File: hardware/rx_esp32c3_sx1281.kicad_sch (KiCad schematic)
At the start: 42 parts, among them U1 ESP32-C3, U3 SX1281IMLTRT, X1 CJ17-400001010B20

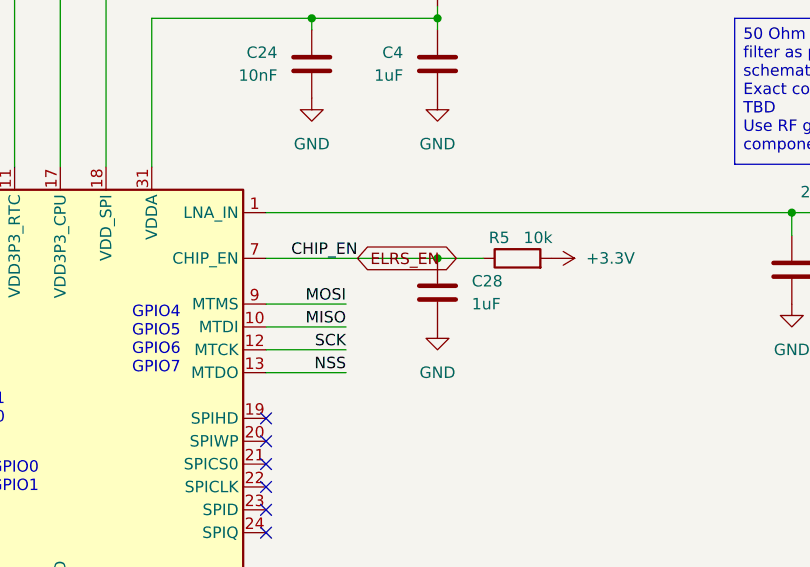
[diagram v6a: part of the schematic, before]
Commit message: ELRS OFF solder jumper JP2 and 1k R115 on CHIP_EN
- JP2 (CHIP_EN to GND, new 1.10 x 0.55 mm footprint
  lib:SolderJumper-2_P0.65mm_Tiny_Open, open mask, no paste): bridging it
  holds the ESP32-C3 in reset with any firmware, so an external receiver on
  J54/J55 or the DJI SBUS on SH-6 pin 6 owns UART1.
- R115 1k between GPIO27 (ELRS_EN) and CHIP_EN: GPIO27 cannot short into a
  bridged jumper (3.3 mA).
- tools/elrs_jumper.py (pcbnew footprint, sexpdata schematic); netlist diff:
  only CHIP_EN/ELRS_EN/GND gain the new pins. ERC 520 -> 519.
- Board synced; JP2, R115, TP42, TP43 parked right of the outline for
  placement (they overlap there: 4 shorting errors until placed).
- R115 has no LCSC number yet.

Co-Authored-By: Claude Opus 5.5 <noreply@anthropic.com>
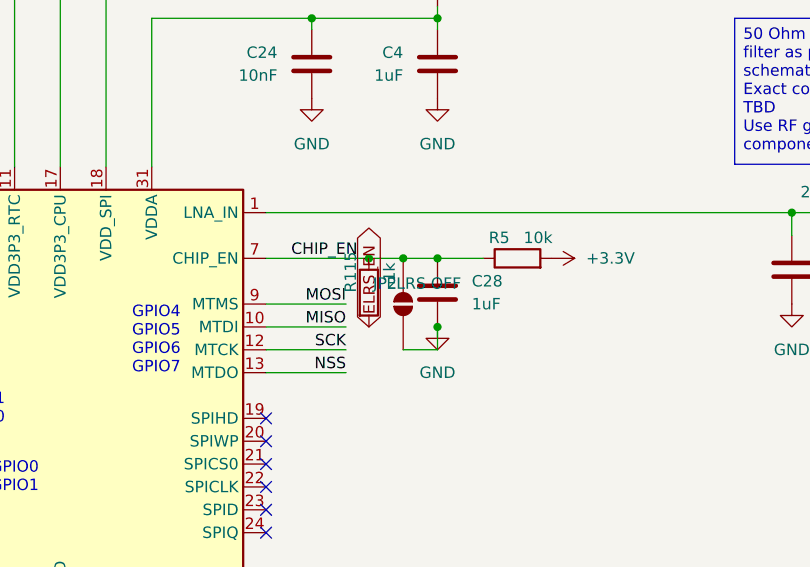
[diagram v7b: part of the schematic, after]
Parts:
- added JP2: ELRS OFF, lib:SolderJumper-2_P0.65mm_Tiny_Open, symbol lib:SolderJumper_2_Open
- added R115: 1k, lib:R_0201_0603Metric, symbol lib:R
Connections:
- net ELRS_EN: now also R115.2; no longer C28.1, R5.1, U1.7 (CHIP_EN)
- net GND: now also JP2.1 (A)
- new net CHIP_EN: C28.1, JP2.2 (B), R115.1, R5.1, U1.7 (CHIP_EN)
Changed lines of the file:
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@@
 	)
 	(junction
+		(at 256.54 205.74)
+		(diameter 0)
+		(color 0 0 0 0)
+	)
+	(junction
 		(at 167.64 233.68)
 		(diameter 0)
@@
 	)
 	(junction
+		(at 264.16 213.36)
+		(diameter 0)
+		(color 0 0 0 0)
+	)
+	(junction
 		(at 138.43 241.3)
 		(diameter 0)
@@
 	)
 	(junction
+		(at 260.35 205.74)
+		(diameter 0)
+		(color 0 0 0 0)
+	)
+	(junction
 		(at 168.91 186.69)
 		(diameter 0)
@@
 	(wire
 		(pts
+			(xy 260.35 215.9) (xy 264.16 215.9)
+		)
+		(stroke
+			(width 0)
+			(type default)
+		)
+	)
+	(wire
+		(pts
 			(xy 279.4 93.98) (xy 279.4 96.52)
 		)
@@
 	(wire
 		(pts
+			(xy 264.16 215.9) (xy 264.16 213.36)
+		)
+		(stroke
+			(width 0)
+			(type default)
+		)
+	)
+	(wire
+		(pts
 			(xy 243.84 166.37) (xy 256.54 166.37)
 		)
@@
 	(global_label "ELRS_EN"
 		(shape bidirectional)
-		(at 255.27 205.74 0)
+		(at 256.54 213.36 90)
 		(effects
 			(font
@@
 		)
 		(property "Intersheetrefs" "${INTERSHEET_REFS}"
-			(at 255.27 205.74 180)
+			(at 256.54 213.36 270)
 			(hide yes)
 			(show_name no)
@@
 	)
 	(symbol
+		(lib_id "lib:R")
+		(at 256.54 209.55 0)
+		(unit 1)
+		(body_style 1)
+		(exclude_from_sim no)
+		(in_bom yes)
+		(on_board yes)
+		(in_pos_files yes)
+		(dnp no)
+		(property "Reference" "R115"
+			(at 254.508 207.264 90)
+			(show_name no)
+			(do_not_autoplace no)
+			(effects
+				(font
+					(size 1.27 1.27)
+				)
+			)
+		)
+		(property "Value" "1k"
+			(at 258.826 207.264 90)
+			(show_name no)
+			(do_not_autoplace no)
+			(effects
+				(font
+					(size 1.27 1.27)
+				)
+			)
+		)
+		(property "Footprint" "lib:R_0201_0603Metric"
+			(at 256.54 211.328 90)
+			(hide yes)
+			(show_name no)
+			(do_not_autoplace no)
+			(effects
+				(font
+					(size 1.27 1.27)
+				)
+			)
+		)
+		(property "Datasheet" ""
+			(at 256.54 209.55 0)
+			(hide yes)
+			(show_name no)
+			(do_not_autoplace no)
+			(effects
+				(font
+					(size 1.27 1.27)
+				)
+			)
+		)
+		(property "Description" "Resistor"
+			(at 256.54 209.55 0)
+			(hide yes)
+			(show_name no)
+			(do_not_autoplace no)
+			(effects
+				(font
+					(size 1.27 1.27)
+				)
+			)
+		)
+		(property "LCSC" ""
+			(at 200.66 356.87 0)
+			(hide yes)
+			(show_name no)
+			(do_not_autoplace no)
+			(effects
+				(font
+					(size 1.27 1.27)
+				)
+			)
+		)
+		(property "LCSC Part" ""
+			(at 200.66 356.87 0)
+			(hide yes)
+			(show_name no)
+			(do_not_autoplace no)
+			(effects
+				(font
+					(size 1.27 1.27)
+				)
+			)
+		)
+		(pin "2"
+		)
+		(pin "1"
+		)
+		(instances
+			(project "OpenAIO"
+				(path "/fb88b6f9-ee39-4640-a9d4-04a17ceeac64/6e8501c6-71d5-4860-9b96-3d3562c097af"
+					(reference "R115")
+					(unit 1)
+				)
+			)
+		)
+	)
+	(symbol
 		(lib_id "lib:GND")
 		(at 153.67 78.74 0)
@@
 					(unit 1)
 				)
+			)
+		)
+	)
+	(symbol
+		(lib_id "lib:SolderJumper_2_Open")
+		(at 260.35 210.82 90)
+		(unit 1)
+		(body_style 1)
+		(exclude_from_sim no)
+		(in_bom yes)
+		(on_board yes)
+		(in_pos_files yes)
+		(dnp no)
+		(property "Reference" "JP2"
+			(at 258.318 208.534 90)
+			(show_name no)
+			(do_not_autoplace no)
+			(effects
+				(font
+					(size 1.27 1.27)
+				)
+			)
+		)
+		(property "Value" "ELRS OFF"
+			(at 262.636 208.534 90)
+			(show_name no)
+			(do_not_autoplace no)
+			(effects
+				(font
+					(size 1.27 1.27)
+				)
+			)
+		)
+		(property "Footprint" "lib:SolderJumper-2_P0.65mm_Tiny_Open"
+			(at 260.35 212.598 90)
+			(hide yes)
+			(show_name no)
+			(do_not_autoplace no)
+			(effects
+				(font
+					(size 1.27 1.27)
+				)
+			)
+		)
+		(property "Datasheet" ""
+			(at 260.35 210.82 0)
+			(hide yes)
+			(show_name no)
+			(do_not_autoplace no)
+			(effects
+				(font
+					(size 1.27 1.27)
+				)
+			)
+		)
+		(property "Description" "Resistor"
+			(at 260.35 210.82 0)
+			(hide yes)
+			(show_name no)
+			(do_not_autoplace no)
+			(effects
+				(font
+					(size 1.27 1.27)
+				)
+			)
+		)
+		(property "LCSC" ""
+			(at 204.47 358.14 0)
+			(hide yes)
+			(show_name no)
+			(do_not_autoplace no)
+			(effects
+				(font
+					(size 1.27 1.27)
+				)
+			)
+		)
+		(property "LCSC Part" ""
+			(at 204.47 358.14 0)
+			(hide yes)
+			(show_name no)
+			(do_not_autoplace no)
+			(effects
+				(font
+					(size 1.27 1.27)
+				)
+			)
+		)
+		(pin "2"
+		)
+		(pin "1"
+		)
+		(instances
+			(project "OpenAIO"
+				(path "/fb88b6f9-ee39-4640-a9d4-04a17ceeac64/6e8501c6-71d5-4860-9b96-3d3562c097af"
+					(reference "JP2")
+					(unit 1)
+				)

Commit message: Owner: routing in progress
Co-Authored-By: Claude Opus 5.5 <noreply@anthropic.com>
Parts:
- renumbered AE1 to AE2, C13 to C65, C12 to C66, C26 to C67, C20 to C68, C19 to C69, C14 to C70, C17 to C71, C1 to C72, C27 to C73, C3 to C74, C11 to C75, C9 to C76, C25 to C77, C5 to C78, C6 to C79, C24 to C80, C23 to C81, C8 to C82, C4 to C83, C28 to C84, C10 to C85, C15 to C86, C22 to C87, C16 to C88, C21 to C89, D1 to D9, L1 to L5, L3 to L6, L2 to L7, R2 to R111, R3 to R112, R4 to R113, R5 to R114, TP5 to TP9, U3 to U21, U1 to U22, X1 to X2
